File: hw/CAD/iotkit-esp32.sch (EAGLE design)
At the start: 4 parts

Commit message: Inkl. Stepper
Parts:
- added (+)STEPPER1: PB0-3, pinhead:PINHD-1X5
- added (+)STEPPER2: PB4-7, pinhead:PINHD-1X5
- added (+)STEPPER3: PA7-4, pinhead:PINHD-1X5
- added 10K: (no value), rcl:R-EU_0204/7
- added IC1: MCP23017SP 0x20, microchip:MCP23017SP
- added S1: PA0, pinhead:PINHD-1X2
- added S2: PA1, pinhead:PINHD-1X2
- added S3: PA2, pinhead:PINHD-1X2
- added STEPPER1, STEPPER2: (no value), SparkFun-IC-Special-Function:ULN2803DIP
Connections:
- new net +5V: (+)STEPPER1.1, (+)STEPPER2.1, (+)STEPPER3.1, STEPPER1.10, STEPPER2.10
- new net N$1: (+)STEPPER2.2, STEPPER1.14
- new net N$2: (+)STEPPER2.3, STEPPER1.13
- new net N$3: (+)STEPPER2.4, STEPPER1.12
- new net N$30: (+)STEPPER1.2, STEPPER1.18
- new net N$31: (+)STEPPER1.3, STEPPER1.17
- new net N$32: (+)STEPPER1.4, STEPPER1.16
- new net N$33: (+)STEPPER1.5, STEPPER1.15
- new net N$4: (+)STEPPER2.5, STEPPER1.11
- new net N$5: 10K.2, IC1.!RESET
- new net N$6: (+)STEPPER3.2, STEPPER2.18
- new net N$7: (+)STEPPER3.3, STEPPER2.17
- new net N$8: (+)STEPPER3.4, STEPPER2.16
- new net N$9: (+)STEPPER3.5, STEPPER2.15
- new net PA0: IC1.GPA0, S1.1
- new net PA1: IC1.GPA1, S2.1
- new net PA2: IC1.GPA2, S3.1
- new net PA4: IC1.GPA4, STEPPER2.4
- new net PA5: IC1.GPA5, STEPPER2.3
- new net PA6: IC1.GPA6, STEPPER2.2
- new net PA7: IC1.GPA7, STEPPER2.1
- new net PB0: IC1.GPB0, STEPPER1.1
- new net PB1: IC1.GPB1, STEPPER1.2
- new net PB2: IC1.GPB2, STEPPER1.3
- new net PB3: IC1.GPB3, STEPPER1.4
- new net PB4: IC1.GPB4, STEPPER1.5
- new net PB5: IC1.GPB5, STEPPER1.6
- new net PB6: IC1.GPB6, STEPPER1.7
- new net PB7: IC1.GPB7, STEPPER1.8
- net 3V3: now also 10K.1, IC1.VDD
- net GND: now also IC1.A0, IC1.A1, IC1.A2, IC1.VSS, S1.2, S2.2, S3.2, STEPPER1.9, STEPPER2.9
- net SCL: now also IC1.SCL
- net SDA: now also IC1.SDA

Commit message: Stepper an 5V
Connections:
- removed net +5V: (+)STEPPER1.1, (+)STEPPER2.1, (+)STEPPER3.1, STEPPER1.10, STEPPER2.10
- net 5V: now also (+)STEPPER1.1, (+)STEPPER2.1, (+)STEPPER3.1, STEPPER1.10, STEPPER2.10
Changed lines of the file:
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@@
 <label x="66.04" y="30.48" size="1.778" layer="95"/>
+</segment>
+<segment>
+<pinref part="SUPPLY1" gate="+5V" pin="+5V"/>
+<pinref part="STEPPER2" gate="G$1" pin="10"/>
+<wire x1="109.22" y1="-22.86" x2="109.22" y2="-27.94" width="0.1524" layer="91"/>
+<wire x1="109.22" y1="-5.08" x2="109.22" y2="-22.86" width="0.1524" layer="91"/>
+<junction x="109.22" y="-22.86"/>
+<pinref part="(+)STEPPER3" gate="A" pin="1"/>
+<wire x1="68.58" y1="-13.97" x2="68.58" y2="-5.08" width="0.1524" layer="91"/>
+<wire x1="68.58" y1="-5.08" x2="109.22" y2="-5.08" width="0.1524" layer="91"/>
+<label x="71.12" y="-7.62" size="1.778" layer="95"/>
+</segment>
+<segment>
+<pinref part="SUPPLY3" gate="+5V" pin="+5V"/>
+<pinref part="STEPPER1" gate="G$1" pin="10"/>
+<wire x1="48.26" y1="-22.86" x2="48.26" y2="-27.94" width="0.1524" layer="91"/>
+<pinref part="(+)STEPPER2" gate="A" pin="1"/>
+<wire x1="30.48" y1="-13.97" x2="30.48" y2="-5.08" width="0.1524" layer="91"/>
+<wire x1="30.48" y1="-5.08" x2="48.26" y2="-5.08" width="0.1524" layer="91"/>
+<wire x1="48.26" y1="-5.08" x2="48.26" y2="-22.86" width="0.1524" layer="91"/>
+<junction x="48.26" y="-22.86"/>
+<pinref part="(+)STEPPER1" gate="A" pin="1"/>
+<wire x1="7.62" y1="-13.97" x2="7.62" y2="-5.08" width="0.1524" layer="91"/>
+<wire x1="7.62" y1="-5.08" x2="30.48" y2="-5.08" width="0.1524" layer="91"/>
+<junction x="30.48" y="-5.08"/>
+<label x="48.26" y="-10.16" size="1.778" layer="95"/>
 </segment>
 </net>
@@
 <pinref part="GND5" gate="1" pin="GND"/>
 <wire x1="48.26" y1="-55.88" x2="48.26" y2="-60.96" width="0.1524" layer="91"/>
+<label x="48.26" y="-60.96" size="1.778" layer="95"/>
 </segment>
 <segment>
@@
 </segment>
 </net>
-<net name="+5V" class="0">
-<segment>
-<pinref part="SUPPLY3" gate="+5V" pin="+5V"/>
-<pinref part="STEPPER1" gate="G$1" pin="10"/>
-<wire x1="48.26" y1="-22.86" x2="48.26" y2="-27.94" width="0.1524" layer="91"/>
-<pinref part="(+)STEPPER2" gate="A" pin="1"/>
-<wire x1="30.48" y1="-13.97" x2="30.48" y2="-5.08" width="0.1524" layer="91"/>
-<wire x1="30.48" y1="-5.08" x2="48.26" y2="-5.08" width="0.1524" layer="91"/>
-<wire x1="48.26" y1="-5.08" x2="48.26" y2="-22.86" width="0.1524" layer="91"/>
-<junction x="48.26" y="-22.86"/>
-<pinref part="(+)STEPPER1" gate="A" pin="1"/>
-<wire x1="7.62" y1="-13.97" x2="7.62" y2="-5.08" width="0.1524" layer="91"/>
-<wire x1="7.62" y1="-5.08" x2="30.48" y2="-5.08" width="0.1524" layer="91"/>
-<junction x="30.48" y="-5.08"/>
-</segment>
-<segment>
-<pinref part="SUPPLY1" gate="+5V" pin="+5V"/>
-<pinref part="STEPPER2" gate="G$1" pin="10"/>
-<wire x1="109.22" y1="-22.86" x2="109.22" y2="-27.94" width="0.1524" layer="91"/>
-<wire x1="109.22" y1="-5.08" x2="109.22" y2="-22.86" width="0.1524" layer="91"/>
-<junction x="109.22" y="-22.86"/>
-<pinref part="(+)STEPPER3" gate="A" pin="1"/>
-<wire x1="68.58" y1="-13.97" x2="68.58" y2="-5.08" width="0.1524" layer="91"/>
-<wire x1="68.58" y1="-5.08" x2="109.22" y2="-5.08" width="0.1524" layer="91"/>
-</segment>
-</net>

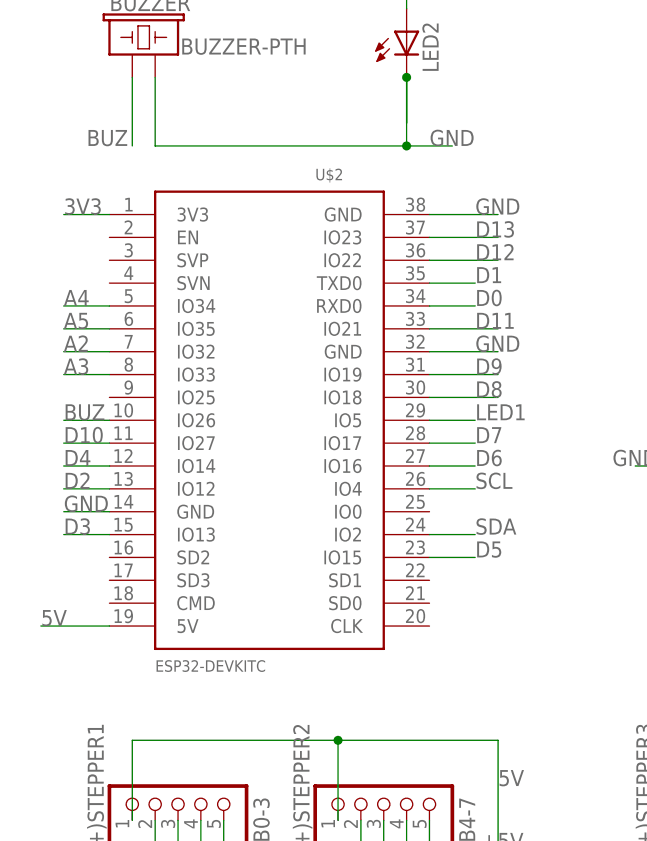
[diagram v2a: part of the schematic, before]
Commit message: Breite ESP32 falsch
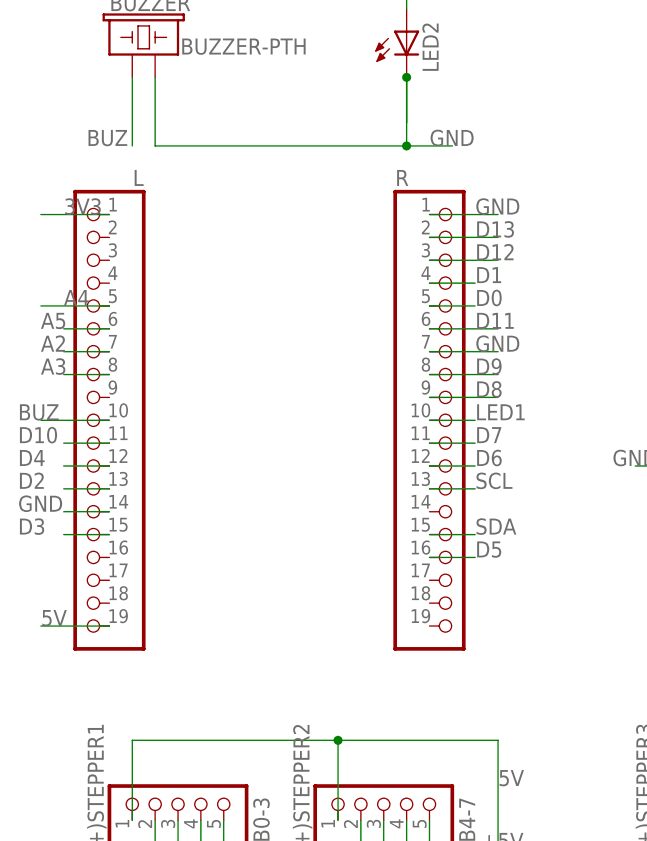
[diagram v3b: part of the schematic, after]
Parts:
- removed U$2: ESP32DEVKITC, relswitch:ESP32DEVKITC
- added L, R: (no value), pinhead:PINHD-1X19
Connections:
- net 3V3: now also L.1; no longer U$2.3V3
- net 5V: now also L.19; no longer U$2.5V
- net A2: now also L.7; no longer U$2.IO32
- net A3: now also L.8; no longer U$2.IO33
- net A4: now also L.5; no longer U$2.IO34
- net A5: now also L.6; no longer U$2.IO35
- net BUZ: now also L.10; no longer U$2.IO26
- net D0: now also R.5; no longer U$2.RXD0
- net D1: now also R.4; no longer U$2.TXD0
- net D10: now also L.11; no longer U$2.IO27
- net D11: now also R.6; no longer U$2.IO21
- net D12: now also R.3; no longer U$2.IO22
- net D13: now also R.2; no longer U$2.IO23
- net D2: now also L.13; no longer U$2.IO12
- net D3: now also L.15; no longer U$2.IO13
- net D4: now also L.12; no longer U$2.IO14
- net D5: now also R.16; no longer U$2.IO15
- net D6: now also R.12; no longer U$2.IO16
- net D7: now also R.11; no longer U$2.IO17
- net D8: now also R.9; no longer U$2.IO18
- net D9: now also R.8; no longer U$2.IO19
- net GND: now also L.14, R.1, R.7; no longer U$2.GND@14, U$2.GND@32, U$2.GND@38
- net LED1: now also R.10; no longer U$2.IO5
- net SCL: now also R.13; no longer U$2.IO4
- net SDA: now also R.15; no longer U$2.IO2

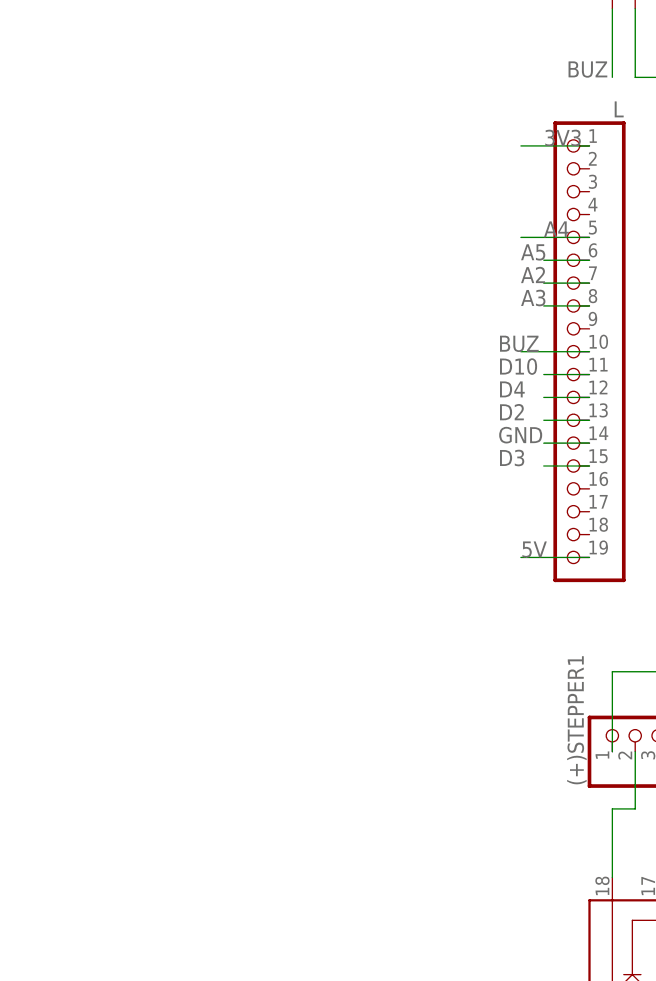
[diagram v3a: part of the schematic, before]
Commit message: M5Stack Core2 Erweiterungen
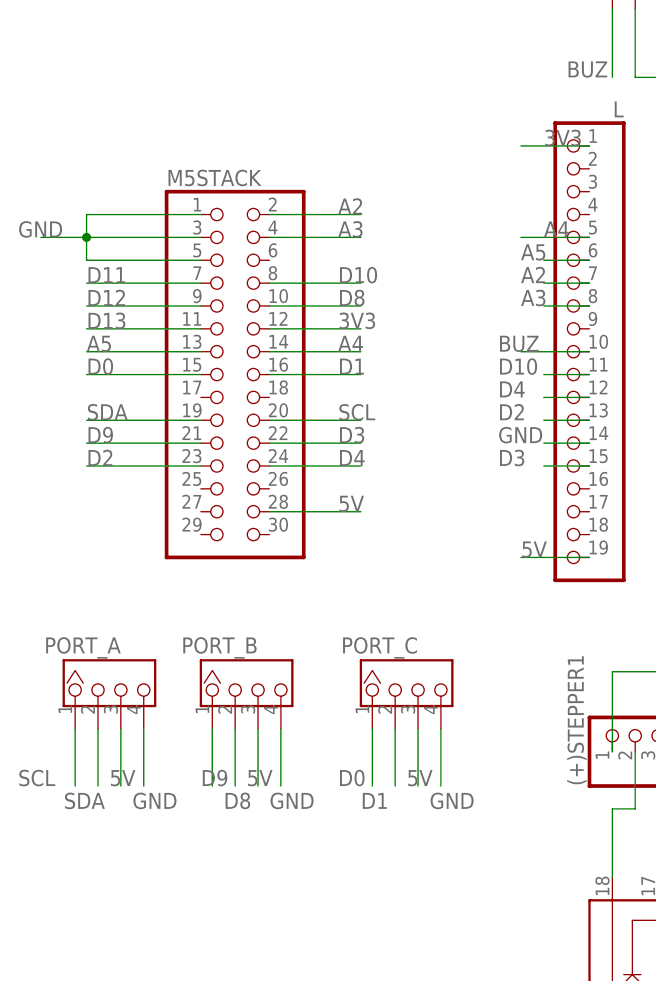
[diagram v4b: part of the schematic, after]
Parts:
- added M5STACK: (no value), pinhead:PINHD-2X15
- added PORT_A, PORT_B, PORT_C: I2C, Seeed-Connector:GROVE-CONNECTOR-DIP(4P-2.0)
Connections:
- net 3V3: now also M5STACK.12
- net 5V: now also M5STACK.28, PORT_A.3, PORT_B.3, PORT_C.3
- net A2: now also M5STACK.2
- net A3: now also M5STACK.4
- net A4: now also M5STACK.14
- net A5: now also M5STACK.13
- net D0: now also M5STACK.15, PORT_C.1
- net D1: now also M5STACK.16, PORT_C.2
- net D10: now also M5STACK.8
- net D11: now also M5STACK.7
- net D12: now also M5STACK.9
- net D13: now also M5STACK.11
- net D2: now also M5STACK.23
- net D3: now also M5STACK.22
- net D4: now also M5STACK.24
- net D8: now also M5STACK.10, PORT_B.2
- net D9: now also M5STACK.21, PORT_B.1
- net GND: now also M5STACK.1, M5STACK.3, M5STACK.5, PORT_A.4, PORT_B.4, PORT_C.4
- net SCL: now also M5STACK.20, PORT_A.1
- net SDA: now also M5STACK.19, PORT_A.2

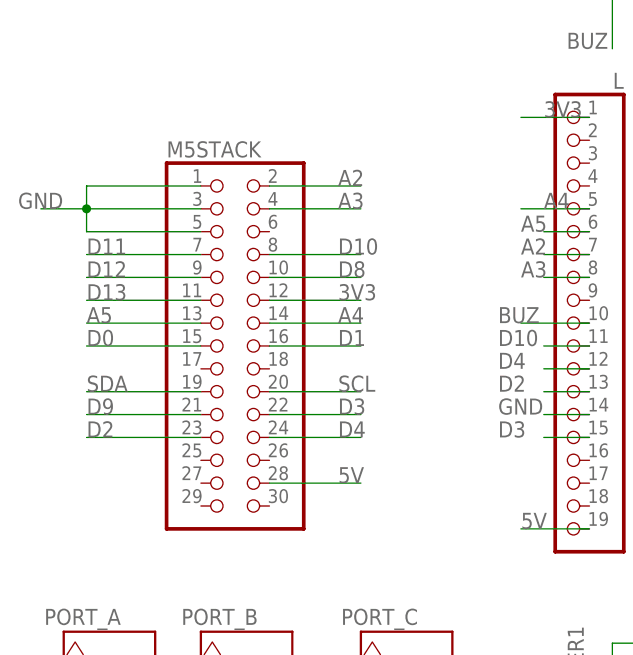
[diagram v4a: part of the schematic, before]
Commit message: M5Stack Seitenverkehrt korr.
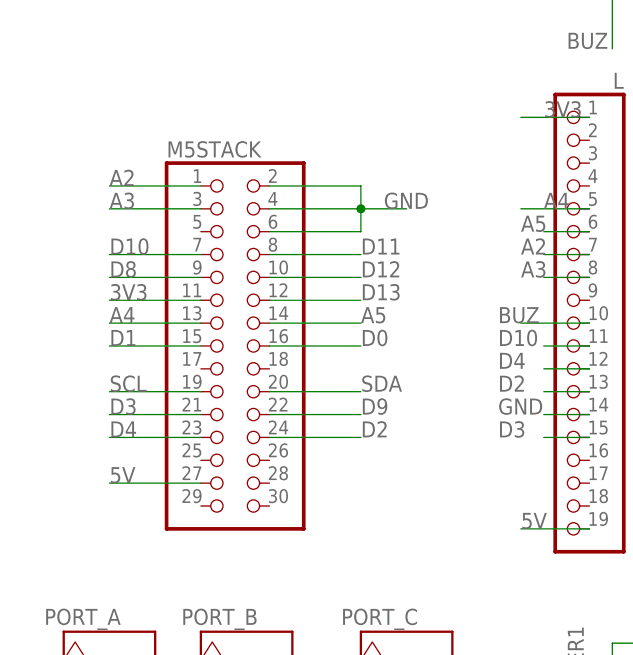
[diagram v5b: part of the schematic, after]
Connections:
- net 3V3: now also M5STACK.11; no longer M5STACK.12
- net 5V: now also M5STACK.27; no longer M5STACK.28
- net A2: now also M5STACK.1; no longer M5STACK.2
- net A3: now also M5STACK.3; no longer M5STACK.4
- net A4: now also M5STACK.13; no longer M5STACK.14
- net A5: now also M5STACK.14; no longer M5STACK.13
- net D0: now also M5STACK.16; no longer M5STACK.15
- net D1: now also M5STACK.15; no longer M5STACK.16
- net D10: now also M5STACK.7; no longer M5STACK.8
- net D11: now also M5STACK.8; no longer M5STACK.7
- net D12: now also M5STACK.10; no longer M5STACK.9
- net D13: now also M5STACK.12; no longer M5STACK.11
- net D2: now also M5STACK.24; no longer M5STACK.23
- net D3: now also M5STACK.21; no longer M5STACK.22
- net D4: now also M5STACK.23; no longer M5STACK.24
- net D8: now also M5STACK.9; no longer M5STACK.10
- net D9: now also M5STACK.22; no longer M5STACK.21
- net GND: now also M5STACK.2, M5STACK.4, M5STACK.6; no longer M5STACK.1, M5STACK.3, M5STACK.5
- net SCL: now also M5STACK.19; no longer M5STACK.20
- net SDA: now also M5STACK.20; no longer M5STACK.19
